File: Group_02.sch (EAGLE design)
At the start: 29 parts, among them J1 POWER_JACKPTH_LOCK, U1 +12v

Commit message: Aggiornamento schematico
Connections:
- new net MUX_A0/1.3C: U$3.A0
- new net MUX_A1/1.4C: U$3.A1
- new net MUX_A2/1.4C: U$3.A2
- new net MUX_OUT/1.4C: U$3.D
- new net N$10: J9.8, U$3.S1
- new net N$11: J9.7, U$3.S2
- new net N$12: J9.6, U$3.S3
- new net N$13: J9.5, U$3.S4
- new net N$14: J9.4, U$3.S5
- new net N$15: J9.3, U$3.S6
- new net N$16: J9.2, U$3.S7
- new net N$17: J9.1, U$3.S8
- net 5V: now also C3.1, U$3.EN, U$3.VDD
- net GND: now also C3.2, U$3.GND
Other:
- moved on the sheet: C3, J9, U$3
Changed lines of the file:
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@@
 <part name="U$2" library="Group_02_Library" deviceset="TCA9546A" device="SMD"/>
 <part name="S1" library="SparkFun-Switches" deviceset="SWITCH-SPDT" device="-PTH-11.6X4.0MM"/>
-<part name="U$3" library="Group_02_Library" deviceset="TMUX1208" device=""/>
 <part name="SUPPLY1" library="SparkFun-PowerSymbols" deviceset="5V" device=""/>
 <part name="SUPPLY2" library="SparkFun-PowerSymbols" deviceset="5V" device=""/>
@@
 <part name="SUPPLY7" library="SparkFun-PowerSymbols" deviceset="5V" device=""/>
 <part name="SUPPLY8" library="SparkFun-PowerSymbols" deviceset="5V" device=""/>
-<part name="SUPPLY9" library="SparkFun-PowerSymbols" deviceset="5V" device=""/>
 <part name="SUPPLY10" library="SparkFun-PowerSymbols" deviceset="5V" device=""/>
 <part name="GND1" library="SparkFun-PowerSymbols" deviceset="GND" device=""/>
@@
 <part name="GND9" library="SparkFun-PowerSymbols" deviceset="GND" device=""/>
 <part name="SUPPLY11" library="SparkFun-PowerSymbols" deviceset="12V" device=""/>
+<part name="U$3" library="Group_02_Library" deviceset="TMUX1208" device=""/>
+<part name="SUPPLY12" library="SparkFun-PowerSymbols" deviceset="5V" device=""/>
 </parts>
 <sheets>
@@
 <attribute name="VALUE" x="95.504" y="155.321" size="1.778" layer="96" font="vector"/>
 </instance>
-<instance part="C3" gate="G$1" x="485.14" y="104.14" smashed="yes">
-<attribute name="NAME" x="486.664" y="107.061" size="1.778" layer="95" font="vector"/>
-<attribute name="VALUE" x="484.124" y="107.061" size="1.778" layer="96" font="vector"/>
+<instance part="C3" gate="G$1" x="485.14" y="91.44" smashed="yes">
+<attribute name="NAME" x="486.664" y="94.361" size="1.778" layer="95" font="vector"/>
+<attribute name="VALUE" x="486.664" y="89.281" size="1.778" layer="96" font="vector"/>
 </instance>
 <instance part="FRAME2" gate="G$1" x="299.72" y="5.08" smashed="yes">
@@
 <attribute name="NAME" x="141.732" y="43.18" size="1.778" layer="95" font="vector" rot="R90"/>
 </instance>
-<instance part="J9" gate="G$1" x="388.62" y="86.36" smashed="yes">
-<attribute name="VALUE" x="383.54" y="73.914" size="1.778" layer="96" font="vector"/>
-<attribute name="NAME" x="383.54" y="99.568" size="1.778" layer="95" font="vector"/>
+<instance part="J9" gate="G$1" x="401.32" y="96.52" smashed="yes">
+<attribute name="VALUE" x="396.24" y="84.074" size="1.778" layer="96" font="vector"/>
+<attribute name="NAME" x="396.24" y="109.728" size="1.778" layer="95" font="vector"/>
 </instance>
 <instance part="D1" gate="G$1" x="109.22" y="58.42" smashed="yes">
@@
 <attribute name="VALUE" x="51.816" y="164.338" size="1.778" layer="96" font="vector" align="top-center"/>
 </instance>
-<instance part="U$3" gate="G$1" x="431.8" y="73.66" smashed="yes">
-<attribute name="NAME" x="435.61" y="115.316" size="2.1844" layer="95"/>
-<attribute name="VALUE" x="435.61" y="70.612" size="2.1844" layer="96"/>
-</instance>
 <instance part="SUPPLY1" gate="G$1" x="106.68" y="175.26" smashed="yes">
 <attribute name="VALUE" x="106.68" y="178.054" size="1.778" layer="96" align="bottom-center"/>
@@
 <attribute name="VALUE" x="182.88" y="76.454" size="1.778" layer="96" align="bottom-center"/>
 </instance>
-<instance part="SUPPLY9" gate="G$1" x="480.06" y="137.16" smashed="yes">
-<attribute name="VALUE" x="480.06" y="139.954" size="1.778" layer="96" align="bottom-center"/>
-</instance>
-<instance part="SUPPLY10" gate="G$1" x="472.44" y="76.2" smashed="yes">
-<attribute name="VALUE" x="472.44" y="78.994" size="1.778" layer="96" align="bottom-center"/>
-</instance>
-<instance part="GND1" gate="1" x="467.36" y="60.96" smashed="yes">
-<attribute name="VALUE" x="467.36" y="60.706" size="1.778" layer="96" align="top-center"/>
+<instance part="SUPPLY10" gate="G$1" x="472.44" y="78.74" smashed="yes">
+<attribute name="VALUE" x="472.44" y="81.534" size="1.778" layer="96" align="bottom-center"/>
+</instance>
+<instance part="GND1" gate="1" x="454.66" y="63.5" smashed="yes">
+<attribute name="VALUE" x="454.66" y="63.246" size="1.778" layer="96" align="top-center"/>
 </instance>
 <instance part="GND2" gate="1" x="167.64" y="53.34" smashed="yes">
@@
 <instance part="SUPPLY11" gate="G$1" x="63.5" y="175.26" smashed="yes">
 <attribute name="VALUE" x="63.5" y="178.054" size="1.778" layer="96" align="bottom-center"/>
+</instance>
+<instance part="U$3" gate="G$1" x="436.88" y="91.44" smashed="yes">
+<attribute name="NAME" x="429.514" y="110.236" size="2.1844" layer="95"/>
+<attribute name="VALUE" x="429.006" y="70.866" size="2.1844" layer="96"/>
+</instance>
+<instance part="SUPPLY12" gate="G$1" x="459.74" y="111.76" smashed="yes">
+<attribute name="VALUE" x="459.74" y="114.554" size="1.778" layer="96" align="bottom-center"/>
 </instance>
 </instances>
@@
 <wire x1="182.88" y1="60.96" x2="182.88" y2="73.66" width="0.1524" layer="91"/>
 <pinref part="SUPPLY8" gate="G$1" pin="5V"/>
+</segment>
+<segment>
+<pinref part="U$3" gate="G$1" pin="EN"/>
+<pinref part="SUPPLY10" gate="G$1" pin="5V"/>
+<wire x1="452.12" y1="78.74" x2="472.44" y2="78.74" width="0.1524" layer="91"/>
+</segment>
+<segment>
+<pinref part="U$3" gate="G$1" pin="VDD"/>
+<wire x1="452.12" y1="106.68" x2="459.74" y2="106.68" width="0.1524" layer="91"/>
+<pinref part="C3" gate="G$1" pin="1"/>
+<wire x1="459.74" y1="106.68" x2="485.14" y2="106.68" width="0.1524" layer="91"/>
+<wire x1="485.14" y1="106.68" x2="485.14" y2="96.52" width="0.1524" layer="91"/>
+<wire x1="459.74" y1="106.68" x2="459.74" y2="111.76" width="0.1524" layer="91"/>
+<junction x="459.74" y="106.68"/>
+<pinref part="SUPPLY12" gate="G$1" pin="5V"/>
 </segment>
 </net>
@@
 <wire x1="96.52" y1="35.56" x2="96.52" y2="30.48" width="0.1524" layer="91"/>
 </segment>
+<segment>
+<pinref part="C3" gate="G$1" pin="2"/>
+<wire x1="485.14" y1="88.9" x2="485.14" y2="76.2" width="0.1524" layer="91"/>
+<wire x1="485.14" y1="76.2" x2="454.66" y2="76.2" width="0.1524" layer="91"/>
+<pinref part="U$3" gate="G$1" pin="GND"/>
+<pinref part="GND1" gate="1" pin="GND"/>
+<wire x1="454.66" y1="76.2" x2="452.12" y2="76.2" width="0.1524" layer="91"/>
+<wire x1="454.66" y1="66.04" x2="454.66" y2="63.5" width="0.1524" layer="91"/>
+<wire x1="454.66" y1="66.04" x2="454.66" y2="76.2" width="0.1524" layer="91"/>
+<junction x="454.66" y="76.2"/>
+</segment>
 </net>
 <net name="12V" class="0">
@@
 </segment>
 </net>
+<net name="N$10" class="0">
+<segment>
+<pinref part="U$3" gate="G$1" pin="S1"/>
+<pinref part="J9" gate="G$1" pin="8"/>
+<wire x1="421.64" y1="106.68" x2="406.4" y2="106.68" width="0.1524" layer="91"/>
+</segment>
+</net>
+<net name="N$11" class="0">
+<segment>
+<pinref part="U$3" gate="G$1" pin="S2"/>
+<pinref part="J9" gate="G$1" pin="7"/>
+<wire x1="421.64" y1="104.14" x2="406.4" y2="104.14" width="0.1524" layer="91"/>
+</segment>
+</net>
+<net name="N$12" class="0">
+<segment>
+<pinref part="J9" gate="G$1" pin="6"/>
+<pinref part="U$3" gate="G$1" pin="S3"/>
+<wire x1="406.4" y1="101.6" x2="421.64" y2="101.6" width="0.1524" layer="91"/>
+</segment>
+</net>
+<net name="N$13" class="0">
+<segment>
+<pinref part="U$3" gate="G$1" pin="S4"/>
+<pinref part="J9" gate="G$1" pin="5"/>
+<wire x1="421.64" y1="99.06" x2="406.4" y2="99.06" width="0.1524" layer="91"/>
+</segment>
+</net>
+<net name="N$14" class="0">
+<segment>
+<pinref part="J9" gate="G$1" pin="4"/>
+<pinref part="U$3" gate="G$1" pin="S5"/>
+<wire x1="406.4" y1="96.52" x2="421.64" y2="96.52" width="0.1524" layer="91"/>
+</segment>
+</net>
+<net name="N$15" class="0">
+<segment>
+<pinref part="U$3" gate="G$1" pin="S6"/>
+<pinref part="J9" gate="G$1" pin="3"/>
+<wire x1="421.64" y1="93.98" x2="406.4" y2="93.98" width="0.1524" layer="91"/>
+</segment>
+</net>
+<net name="N$16" class="0">
+<segment>
+<pinref part="J9" gate="G$1" pin="2"/>
+<pinref part="U$3" gate="G$1" pin="S7"/>
+<wire x1="406.4" y1="91.44" x2="421.64" y2="91.44" width="0.1524" layer="91"/>
+</segment>
+</net>
+<net name="N$17" class="0">
+<segment>
+<pinref part="U$3" gate="G$1" pin="S8"/>
+<pinref part="J9" gate="G$1" pin="1"/>
+<wire x1="421.64" y1="88.9" x2="406.4" y2="88.9" width="0.1524" layer="91"/>
+</segment>
+</net>
+<net name="MUX_OUT/1.4C" class="0">
+<segment>
+<pinref part="U$3" gate="G$1" pin="D"/>
+<wire x1="452.12" y1="86.36" x2="454.66" y2="86.36" width="0.1524" layer="91"/>
+<label x="454.66" y="86.36" size="1.778" layer="95" xref="yes"/>
+</segment>
+</net>
+<net name="MUX_A0/1.3C" class="0">
+<segment>
+<pinref part="U$3" gate="G$1" pin="A0"/>
+<wire x1="421.64" y1="81.28" x2="403.86" y2="81.28" width="0.1524" layer="91"/>
+<label x="403.86" y="81.28" size="1.778" layer="95" rot="R180" xref="yes"/>
+</segment>
+</net>
+<net name="MUX_A1/1.4C" class="0">
+<segment>
+<pinref part="U$3" gate="G$1" pin="A1"/>
+<wire x1="421.64" y1="78.74" x2="403.86" y2="78.74" width="0.1524" layer="91"/>
+<label x="403.86" y="78.74" size="1.778" layer="95" rot="R180" xref="yes"/>
+</segment>
+</net>
+<net name="MUX_A2/1.4C" class="0">
+<segment>
+<pinref part="U$3" gate="G$1" pin="A2"/>
+<wire x1="421.64" y1="76.2" x2="403.86" y2="76.2" width="0.1524" layer="91"/>
+<label x="403.86" y="76.2" size="1.778" layer="95" rot="R180" xref="yes"/>
+</segment>
+</net>

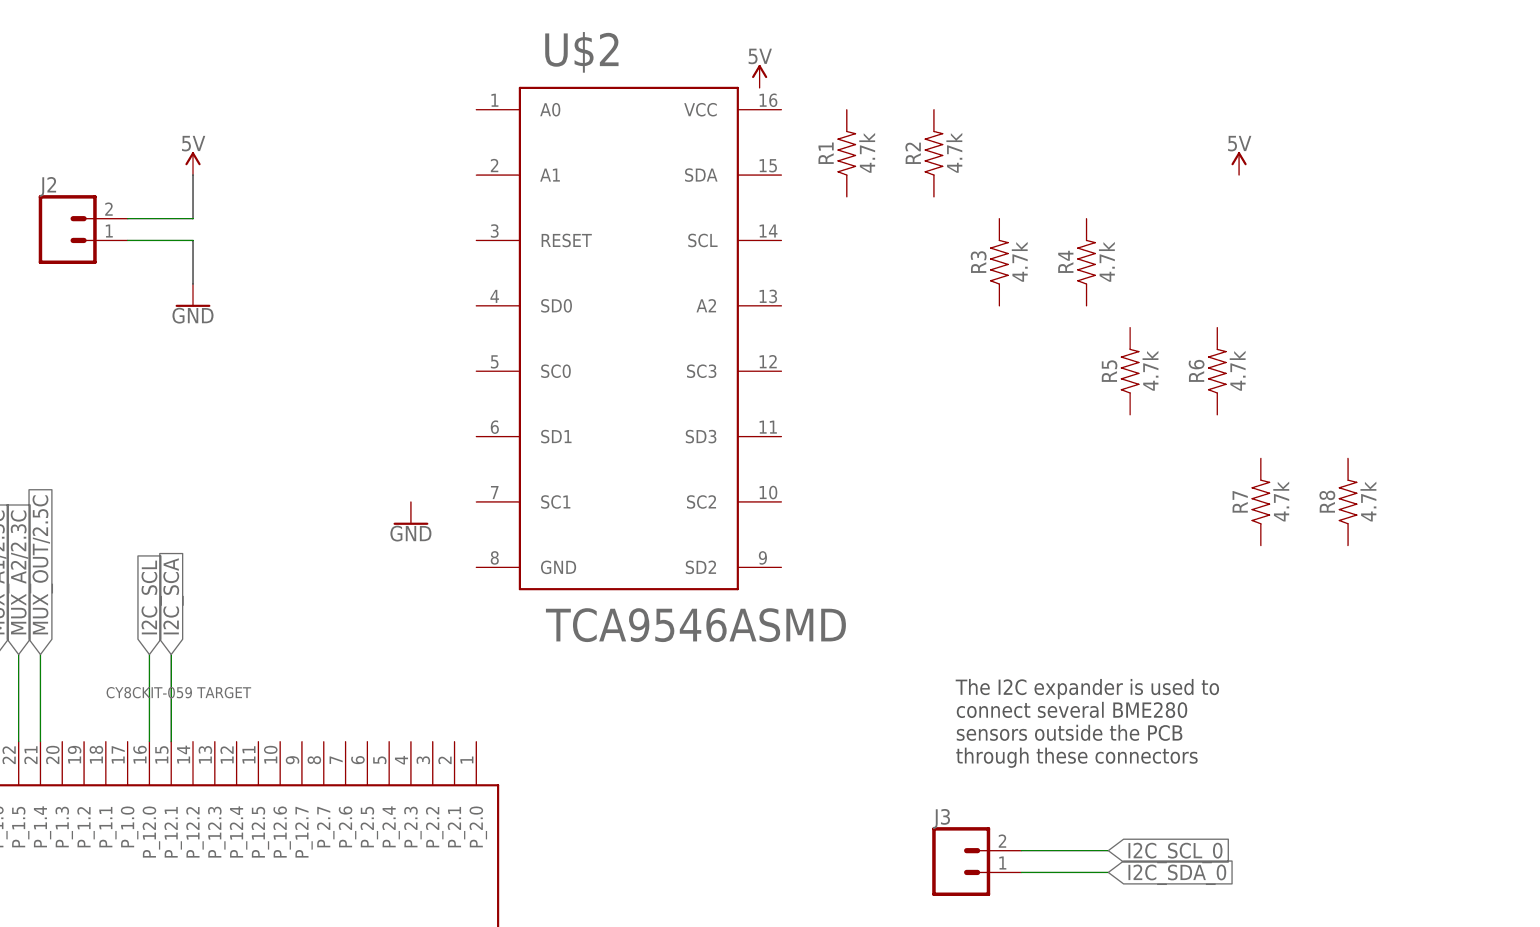
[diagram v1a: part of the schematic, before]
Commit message: Completamento schematico con tca
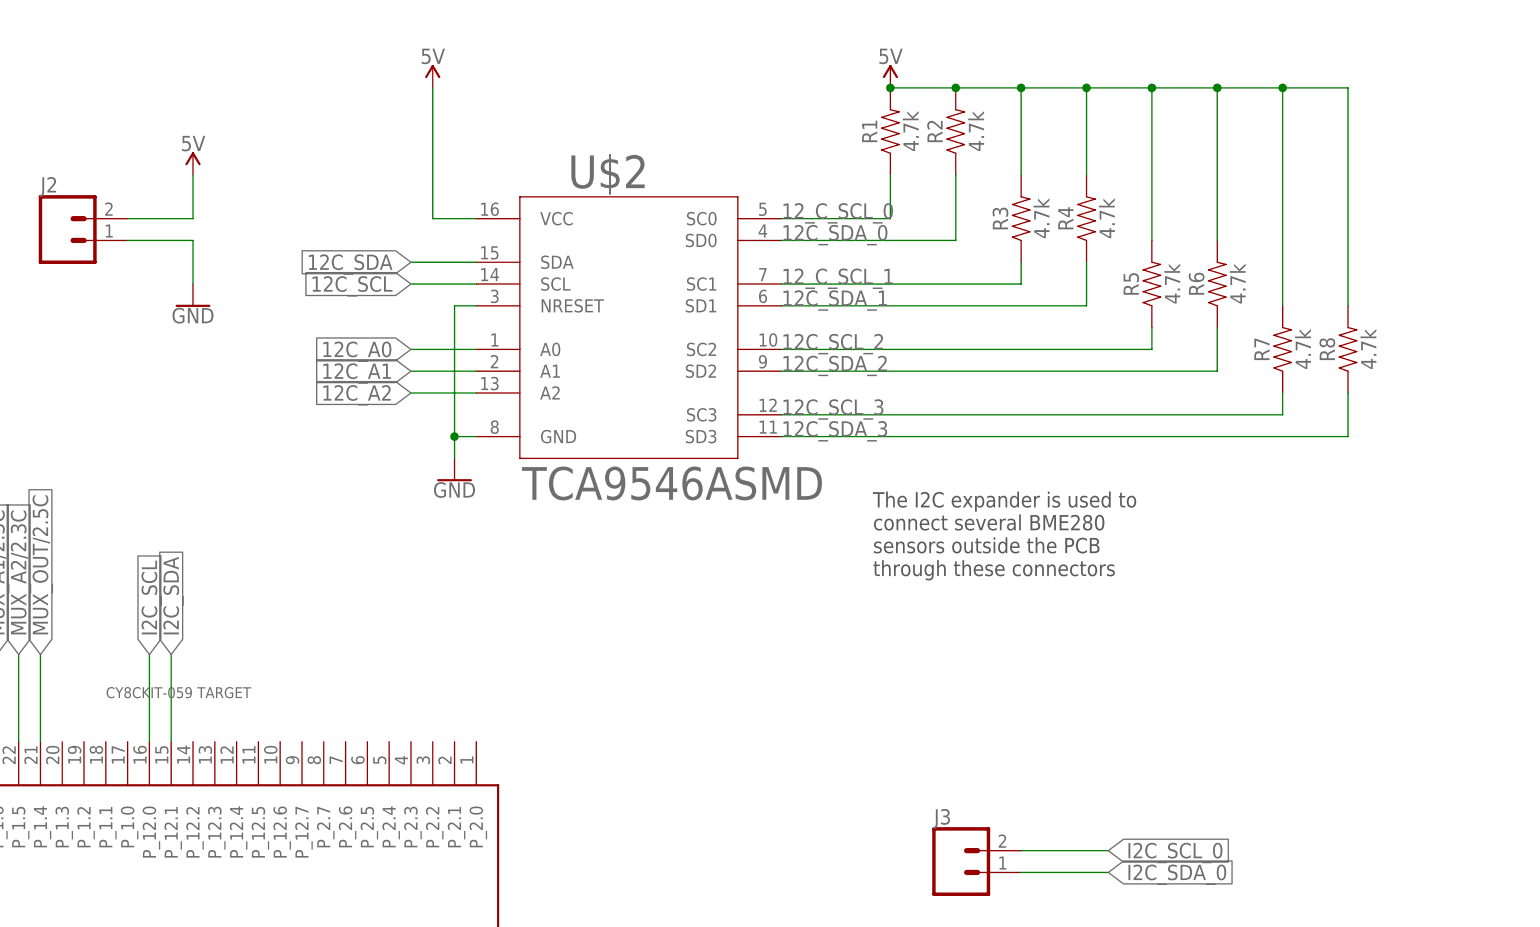
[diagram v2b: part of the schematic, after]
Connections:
- net I2C_SCA renamed I2C_SDA
- new net 12C_A0: U$2.A0
- new net 12C_A1: U$2.A1
- new net 12C_A2: U$2.A2
- new net 12C_SCL: U$2.SCL
- new net 12C_SCL_2: R5.1, U$2.SC2
- new net 12C_SCL_3: R7.1, U$2.SC3
- new net 12C_SDA: U$2.SDA
- new net 12C_SDA_0: R2.1, U$2.SD0
- new net 12C_SDA_1: R4.1, U$2.SD1
- new net 12C_SDA_2: R6.1, U$2.SD2
- new net 12C_SDA_3: R8.1, U$2.SD3
- new net 12_C_SCL_0: R1.1, U$2.SC0
- new net 12_C_SCL_1: R3.1, U$2.SC1
- net 5V: now also R1.2, R2.2, R3.2, R4.2, R5.2, R6.2, R7.2, R8.2, U$2.VCC
- net GND: now also U$2.GND, U$2.NRESET
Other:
- moved on the sheet: R1, R2, R3, R4, R5, R6, R7, R8, U$2
